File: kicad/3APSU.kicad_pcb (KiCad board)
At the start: 2 copper layers, 178 x 127 mm, 55 parts, among them P1 9VAC, P10 -12V, P2 9VAC, P3 15VAC, P4 GND, P5 15VAC, P6 +5V, P7 0V, P8 +12V, P9 -5V, U1 LM323K, U2 L7812, U3 L7905, U4 L7912

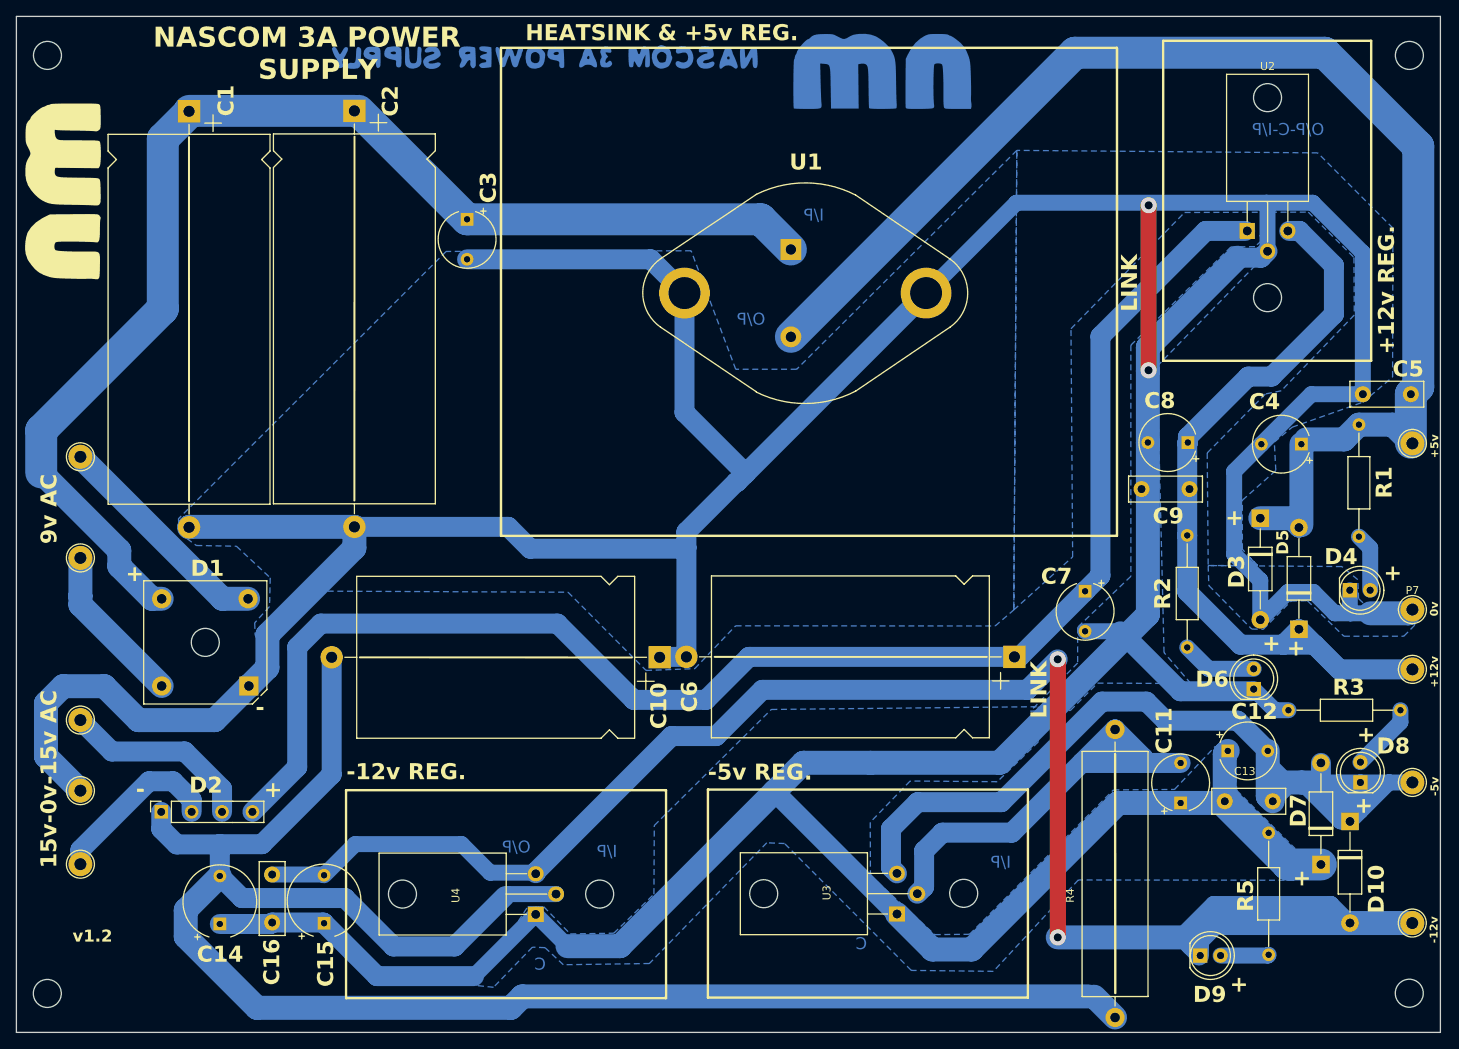
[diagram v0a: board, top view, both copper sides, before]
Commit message: Kicad 9 update
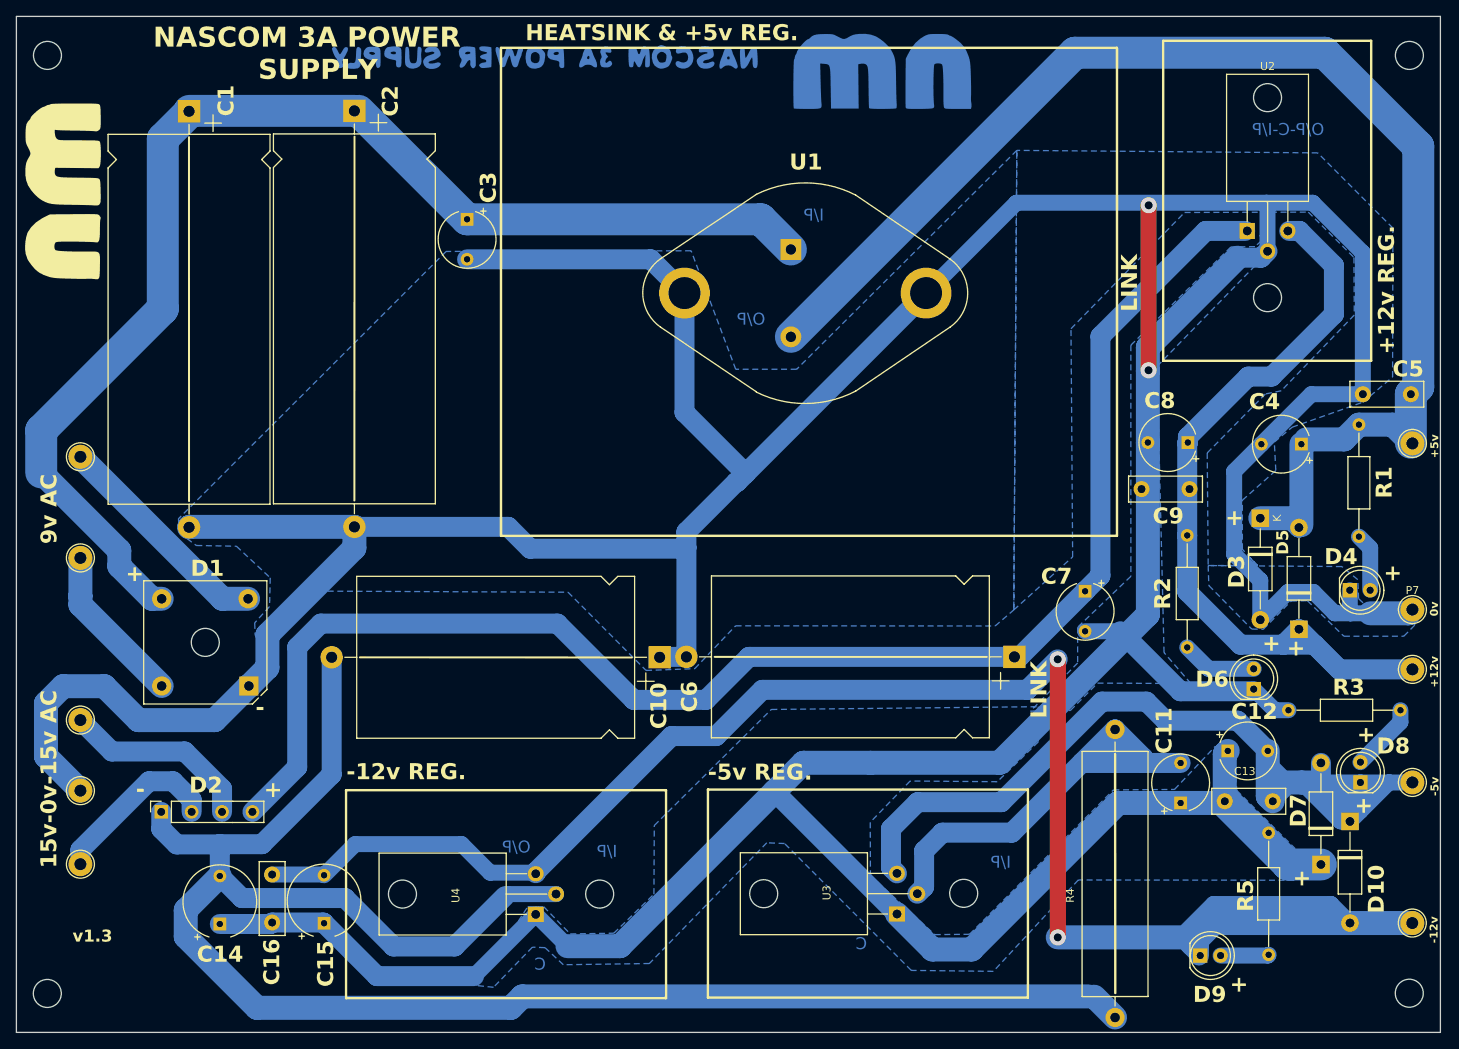
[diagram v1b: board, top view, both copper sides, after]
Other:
- board text added: "v1.3"
- board text removed: "v1.2"

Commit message: Add code
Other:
- board text added: "CS-012"
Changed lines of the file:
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@@
+		)
+	)
+	(gr_text "CS-012"
+		(at 215.909879 172.802291 0)
+		(layer "B.SilkS")
+		(effects
+			(font
+				(size 1 1)
+				(thickness 0.15)
+			)
+			(justify left bottom mirror)
 		)
 	)
